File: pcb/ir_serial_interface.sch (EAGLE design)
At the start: 33 parts, among them IC1 PIC18LF2550, IC2 LP2992, T1 PS401

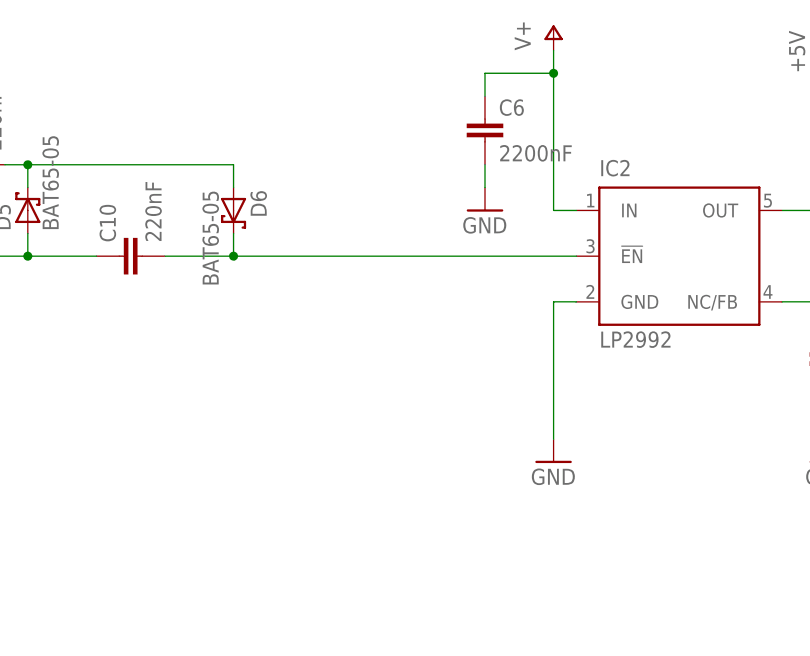
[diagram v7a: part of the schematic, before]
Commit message: PCB: with zener and serial on ICSP
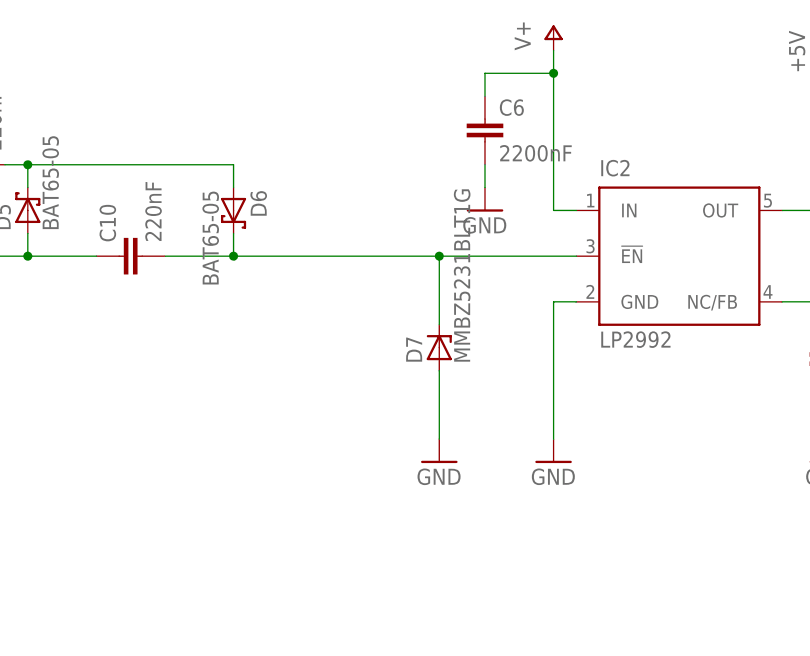
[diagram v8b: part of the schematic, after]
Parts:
- added D7: MMBZ5231BLT1G, diode:ZENER-DIODESOT23
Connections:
- net GND: now also D7.A
- net N$21: now also D7.C
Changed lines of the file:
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@@
 <part name="C9" library="rcl" deviceset="C-EU" device="C0805" value="220nF"/>
 <part name="C10" library="rcl" deviceset="C-EU" device="C0805" value="220nF"/>
+<part name="D7" library="diode" deviceset="ZENER-DIODE" device="SOT23" value="MMBZ5231BLT1G"/>
+<part name="GND20" library="supply1" deviceset="GND" device=""/>
 <part name="P+8" library="supply1" deviceset="+5V" device=""/>
 </parts>
@@
 <instance part="C9" gate="G$1" x="177.8" y="99.06" rot="R90"/>
 <instance part="C10" gate="G$1" x="195.58" y="88.9" rot="R90"/>
+<instance part="D7" gate="G$1" x="231.14" y="78.74" rot="R90"/>
+<instance part="GND20" gate="1" x="231.14" y="66.04"/>
 <instance part="P+8" gate="1" x="33.02" y="38.1"/>
 </instances>
@@
 <wire x1="149.86" y1="88.9" x2="157.48" y2="88.9" width="0.1524" layer="91"/>
 <junction x="149.86" y="88.9"/>
+</segment>
+<segment>
+<pinref part="D7" gate="G$1" pin="A"/>
+<pinref part="GND20" gate="1" pin="GND"/>
+<wire x1="231.14" y1="76.2" x2="231.14" y2="68.58" width="0.1524" layer="91"/>
 </segment>
 </net>
@@
 <junction x="208.28" y="88.9"/>
 <pinref part="IC2" gate="G$1" pin="!EN"/>
-<wire x1="246.38" y1="88.9" x2="208.28" y2="88.9" width="0.1524" layer="91"/>
-</segment>
-</net>
+<wire x1="246.38" y1="88.9" x2="231.14" y2="88.9" width="0.1524" layer="91"/>
+<pinref part="D7" gate="G$1" pin="C"/>
+<wire x1="231.14" y1="88.9" x2="208.28" y2="88.9" width="0.1524" layer="91"/>
+<wire x1="231.14" y1="81.28" x2="231.14" y2="88.9" width="0.1524" layer="91"/>
+<junction x="231.14" y="88.9"/>
+</segment>
+</net>
